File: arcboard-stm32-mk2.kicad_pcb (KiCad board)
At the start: 2 copper layers, 60 x 60 mm, 92 parts, among them J1 Conn_01x04_Socket, J17 Conn_01x04_Socket, J2 Conn_01x04_Socket, J3 Conn_01x04_Socket, J4 Conn_01x02_Socket, J5 Conn_01x02_Socket, J6 Conn_01x02_Socket, J7 Conn_01x02_Socket, J8 Conn_01x02_Socket, U1 XC6210B332MR-G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

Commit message: top silkscreen good enough for now
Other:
- board text added: "ffc traces facing pcb"

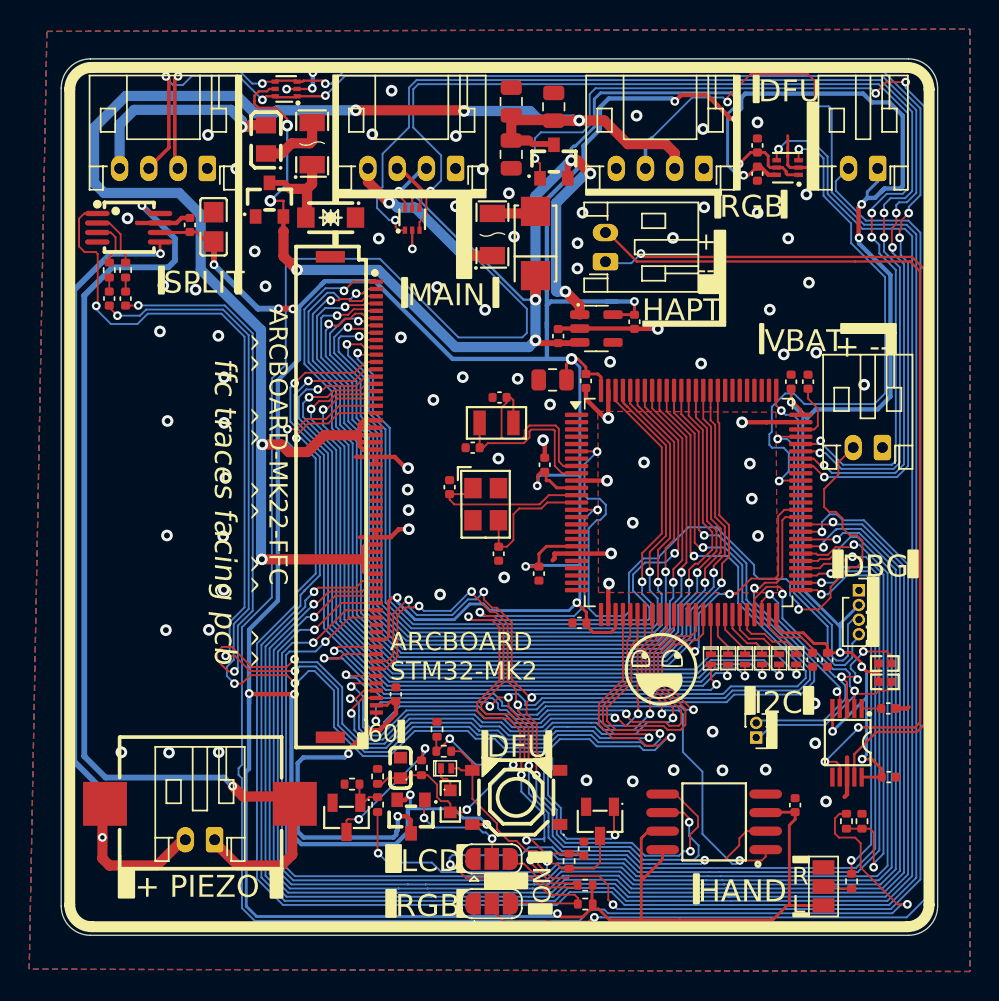
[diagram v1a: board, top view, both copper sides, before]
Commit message: silkscreen mostly done, fixed some DRC issues
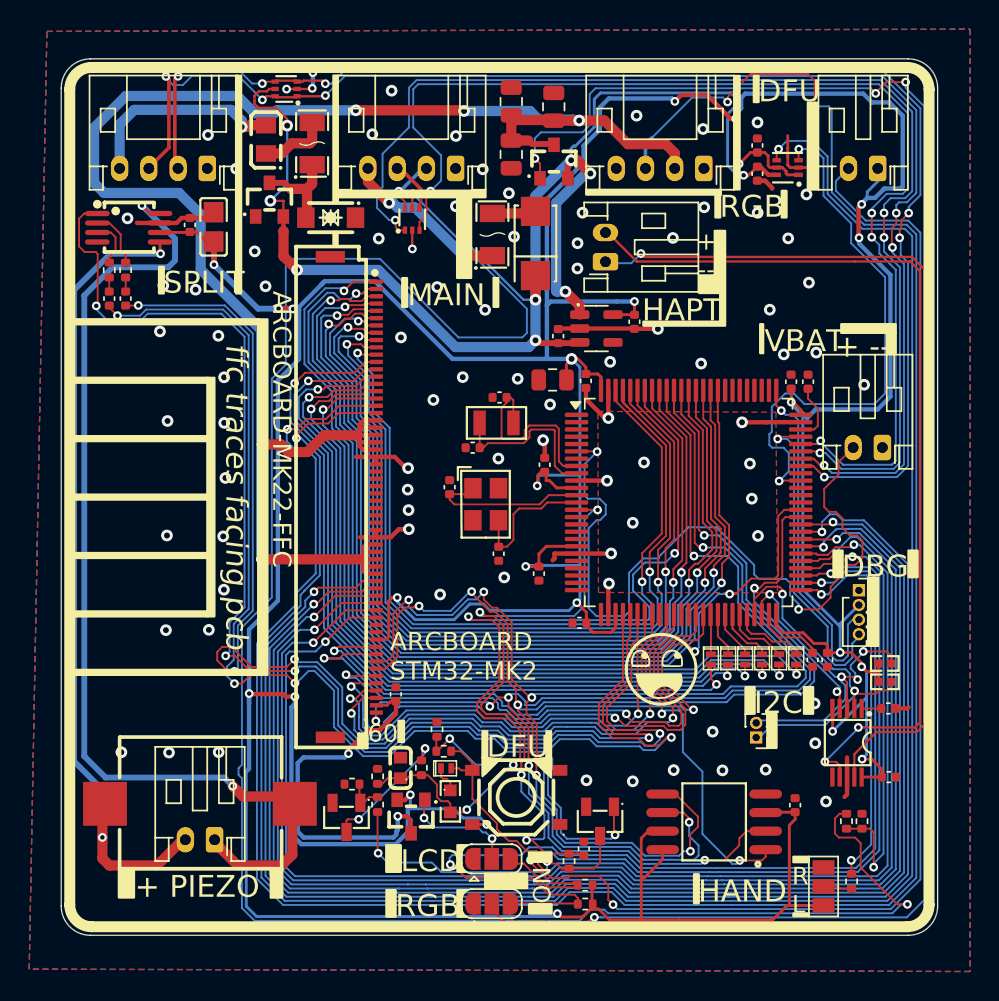
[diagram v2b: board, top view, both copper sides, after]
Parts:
- moved LOGO3 16.4 mm to (74.3, 99.5), turned to 0 degrees
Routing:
- net GND: track 49.5 -> 52.6 mm
- net +3V3: track 375.8 -> 374.5 mm
- net NRST: track 42.9 -> 42.2 mm
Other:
- board text added: "- STM32F405 - 16MB SPI Flash - Haptic DRV2605L - DAC Amp PAM8302A - 32MHz LSE for RTC - VBAT 1.6-3.3v"
- board text added: "ARCBOARD-MK22-FFC"
- board text added: "BOOT/RESET 3V3 DFU"
- board text added: "Boot: hold for 3s Reset: momentary"
- board text added: "EXT RGB G 5V LED x"
- board text added: "HAP+ HAP-"
- board text added: "MAIN USB G DM DP 5V"
- board text added: "PIEZO"
- board text added: "SPLIT USB G TX RX VBUS"
- board text added: "Using JST-PH connectors"
- board text removed: "ARCBOARD-MK22-FFC ^^ ^^ ^^ ^^ ^^"

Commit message: tidying up ground planes, traces
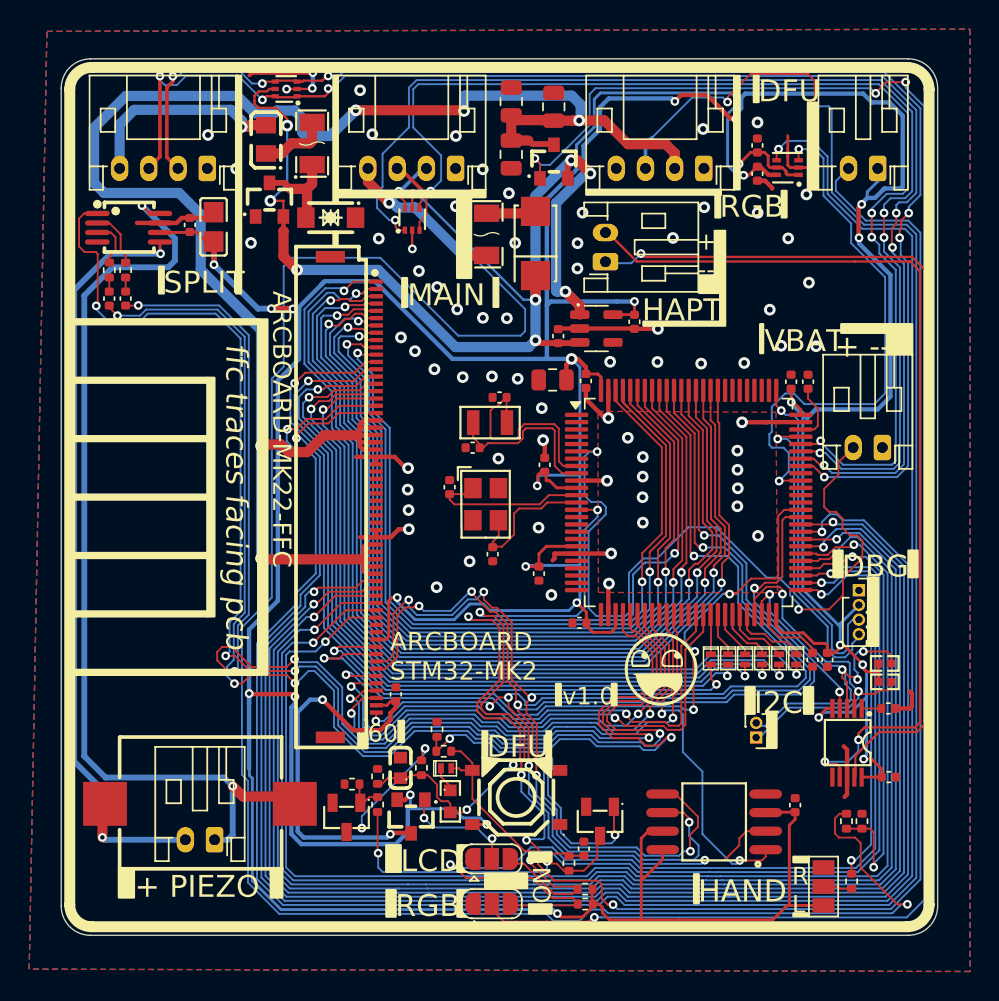
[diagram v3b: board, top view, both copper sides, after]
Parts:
- moved U8 0.44 mm to (99.4, 94.9)
- moved C6 0.41 mm to (99.5, 103.9)
- moved F1 0.40 mm to (99.1, 82.0)
- moved R8 0.27 mm to (105.9, 126.8)
- moved R14 0.15 mm to (104.8, 125.1)
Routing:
- net GND: track 52.6 -> 59.2 mm, vias 88 -> 73
- net VO-: track 71.1 -> 65.5 mm
- net RGB_5V: track 117.9 -> 122.2 mm
- net PMW_MOTION: track 52.3 -> 49.2 mm
- net LCD_RST: track 41.2 -> 38.6 mm
- net AMP_IN+: track 86.2 -> 88.8 mm
- net PMW_CS: track 41.1 -> 38.9 mm
- net AMP_IN-: track 83.1 -> 85.3 mm
- net VO+: track 57.2 -> 55.1 mm
- net VBUS: track 139.9 -> 138.0 mm
- net AMP_SD: track 91.2 -> 93.0 mm
- net BOOT0: track 59.6 -> 57.8 mm
- net I2C_SDA: track 26.5 -> 28.2 mm
- net ROW10: track 56.0 -> 54.5 mm
- net LCD_3V3: track 25.5 -> 27.0 mm
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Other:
- board text added: "v1.0"

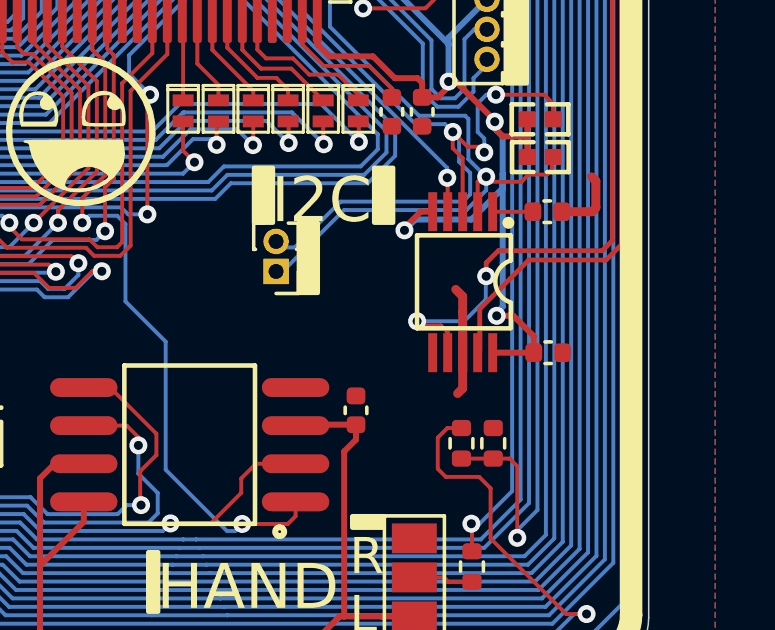
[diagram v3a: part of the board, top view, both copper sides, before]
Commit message: fixing haptic driver missing another vdd, more
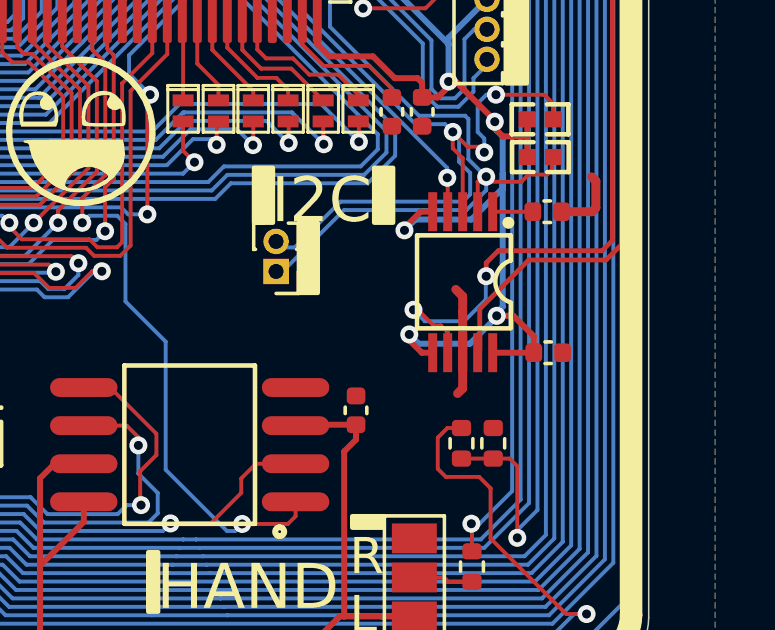
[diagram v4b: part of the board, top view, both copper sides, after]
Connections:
- U5 pad 6: unconnected-(U5-VDD/NC-Pad6) -> +3V3
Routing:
- net +3V3: track 374.3 -> 378.9 mm, vias 24 -> 25
- net HAPTIC_pos: track 63.7 -> 64.3 mm

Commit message: moving i2c breakout to not interfere with rear silkscreen, moving piezo b.silk label
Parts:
- moved J6 2.83 mm to (114.8, 116.1)
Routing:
- net I2C_SDA: track 28.2 -> 31.0 mm
- net I2C_SCL: track 26.5 -> 29.1 mm

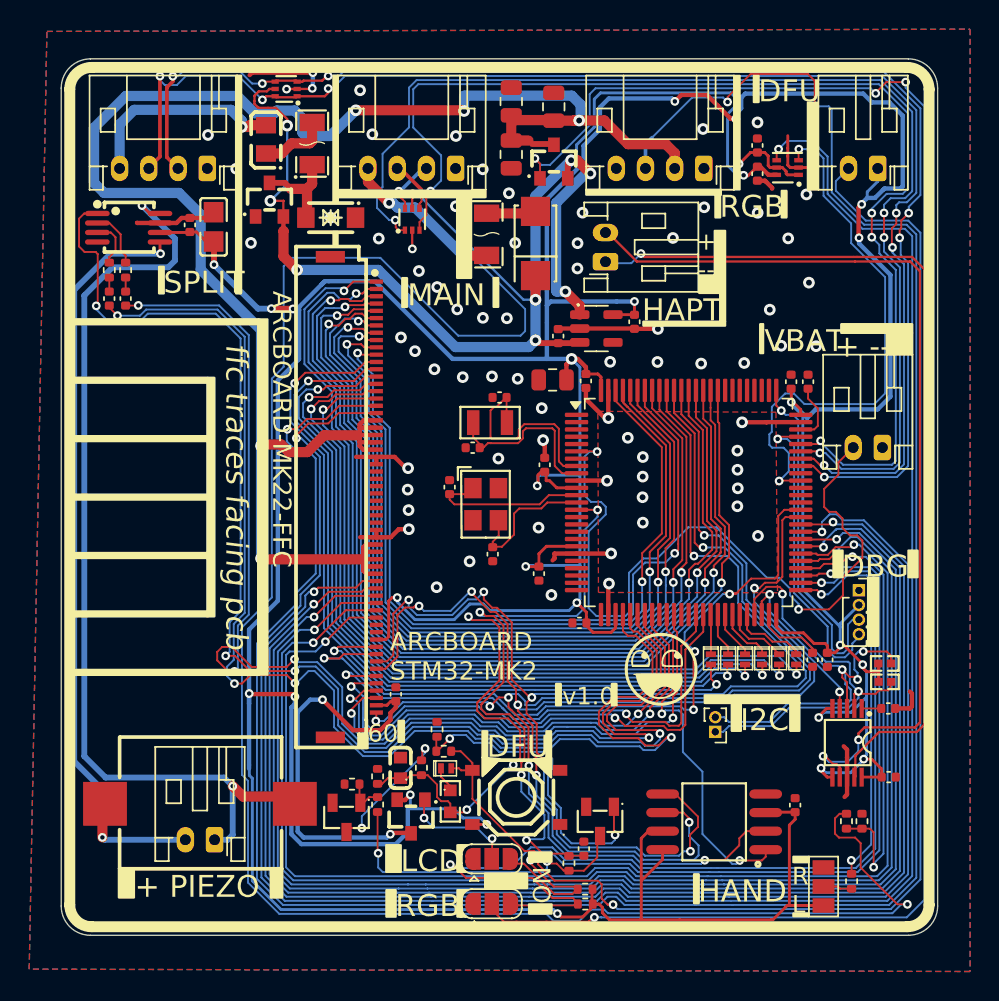
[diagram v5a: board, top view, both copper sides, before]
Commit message: refactoring rgb-lcd power to match tzarc, old way was fundamentally broken
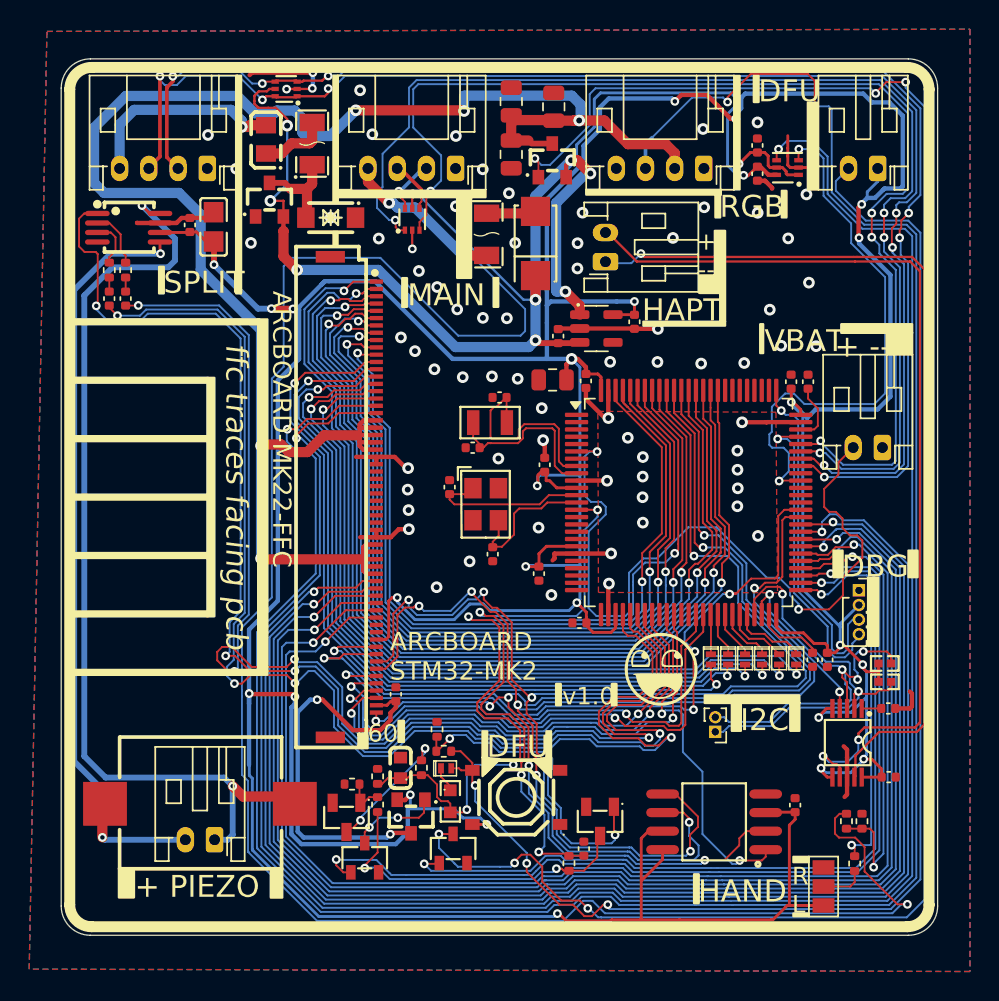
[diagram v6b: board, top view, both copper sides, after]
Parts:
- removed JP1, JP4: SolderJumper_3_Open, Jumper:SolderJumper-3_P1.3mm_Open_RoundedPad1.0x1.5mm
- removed MOSFET2: AO3401A, kicad-libraries:SOT-23_L2.9-W1.3-P1.90-LS2.4-BR
- removed R7, R8: 10k, Resistor_SMD:R_0402_1005Metric
- added MOSFET4: AO3401A, kicad-libraries:SOT-23_L2.9-W1.3-P1.90-LS2.4-BR, F.Cu at (103.6, 77.0)
- added U10: MMUN2233LT1G, kicad-libraries:SOT-23-3_L2.9-W1.3-P1.90-LS2.4-BR, F.Cu at (96.8, 124.1)
- added U9: MMUN2233LT1G, kicad-libraries:SOT-23-3_L2.9-W1.3-P1.90-LS2.4-BR, F.Cu at (90.8, 124.7)
- moved R12 1.23 mm to (124.3, 125.1)
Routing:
- net Net-(MOSFET4-G): track 0.00 -> 126.3 mm, vias 0 -> 6
- net Net-(JP1-C): track 118.8 -> 0.00 mm, vias 4 -> 0
- net RGB_ON: track 70.2 -> 57.6 mm
- net LCD_ON: track 60.1 -> 65.3 mm
- net +3V3: track 378.9 -> 375.7 mm
- net Net-(MOSFET3-G): track 7.95 -> 6.31 mm
- net NRST: track 41.8 -> 40.5 mm
- net BOOT0: track 57.8 -> 59.0 mm
- net Net-(JP3-C): track 1.98 -> 3.01 mm
- net Net-(U13-D): track 21.7 -> 22.7 mm
- net LED_EXT_DI: track 163.2 -> 162.4 mm
- net LED_KEYS_DI: track 143.5 -> 142.6 mm
- net ENCODER3_R1: track 102.2 -> 101.3 mm
- net ENCODER1_R2: track 91.1 -> 90.3 mm
- net VBUS: track 138.0 -> 137.3 mm
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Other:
- board text removed: "LCD"
- board text removed: "ON"

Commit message: silkscreen refactoring and moving bits around
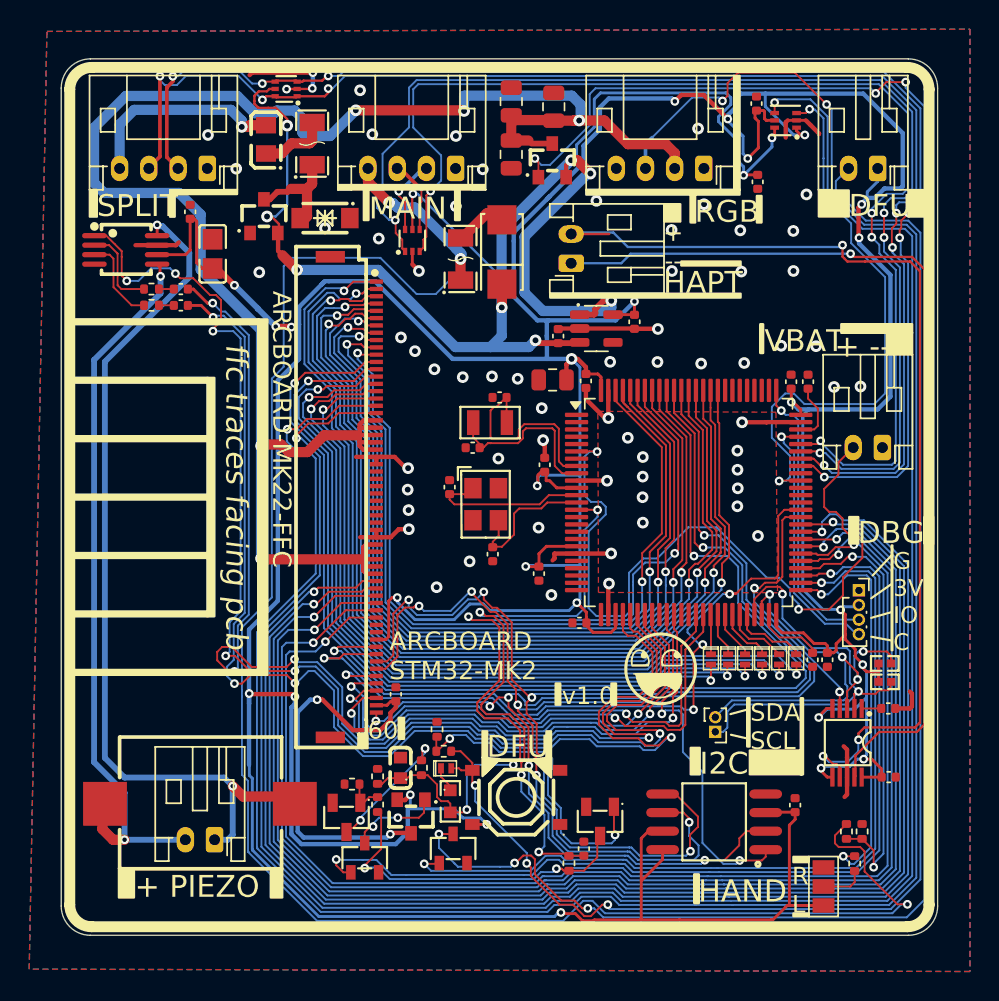
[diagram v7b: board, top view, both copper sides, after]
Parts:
- moved C28 4.92 mm to (78.2, 86.9), turned to 0 degrees
- moved C26 3.84 mm to (78.2, 85.8), turned to 0 degrees
- moved R17 3.76 mm to (76.2, 86.9), turned to 180 degrees
- moved LED-LVL1 3.23 mm to (119.6, 74.2)
- moved C18 2.87 mm to (117.6, 73.1)
- moved F1 2.45 mm to (97.3, 83.7)
- moved D1 2.37 mm to (100.2, 83.2)
- moved J7 2.35 mm to (104.9, 84.0)
- moved R5 2.20 mm to (76.2, 85.8), turned to 180 degrees
- moved C25 1.85 mm to (80.4, 83.3)
- moved U6 1.53 mm to (74.4, 83.1)
- moved D7 1.45 mm to (94.0, 82.4)
- moved MOSFET1 1.19 mm to (83.9, 80.8)
- moved C24 0.90 mm to (78.8, 80.5)
- moved R11 0.70 mm to (124.8, 122.9)
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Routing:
- net +5V: track 104.9 -> 117.6 mm, vias 10 -> 11
- net VBUS: track 137.3 -> 125.4 mm
- net +3V3: track 375.7 -> 386.1 mm, vias 25 -> 26
- net VO-: track 65.5 -> 59.5 mm
- net AMP_IN+: track 88.8 -> 83.0 mm
- net HAPTIC_pos: track 64.3 -> 69.8 mm, vias 2 -> 3
- net VO+: track 55.1 -> 50.9 mm
- net SWCLK: track 23.5 -> 19.6 mm
- net AMP_IN-: track 85.3 -> 81.5 mm
- net GND: track 59.2 -> 55.6 mm, vias 73 -> 65
- net SWDIO: track 21.3 -> 18.0 mm
- net AMP_SD: track 93.0 -> 89.7 mm, vias 4 -> 6
- net LED_KEYS_DI: track 142.6 -> 145.5 mm
- net Net-(U6-IN+): track 3.30 -> 5.97 mm
- net HAPTIC_neg: track 60.9 -> 63.2 mm
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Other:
- board text added: "+PIEZO"
- board text added: "G 3V IO C"
- board text added: "SDA SCL"
- board text added: "github.com/christrotter/arcboard-stm32-mk2"
- board text removed: "PIEZO"
